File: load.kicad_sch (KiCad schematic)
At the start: 42 parts, among them IC3 TC4429CPA, IC4 TPS2121RUXR, J12 Conn_01x02_Socket, J13 Conn_01x02_Socket, J14 Conn_01x02_Socket, J16 Conn_01x02_Socket, J24 Conn_01x02_Socket, J3 Conn_01x02_Socket, J5 Conn_01x02_Socket, J9 Conn_01x03_Socket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

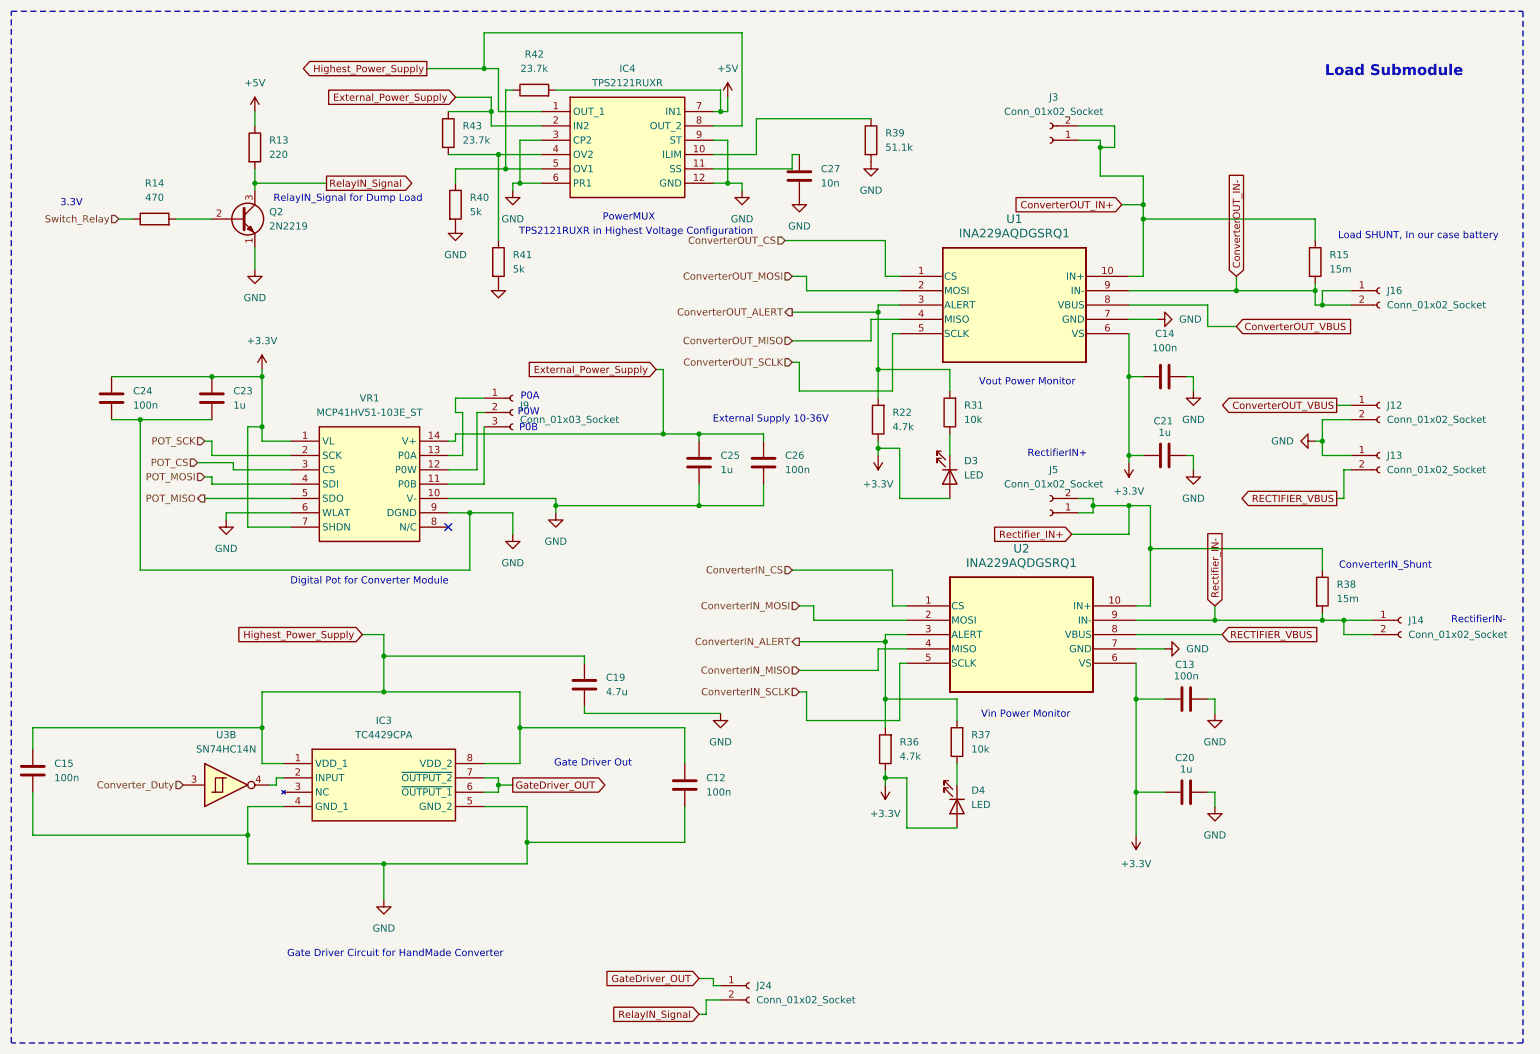
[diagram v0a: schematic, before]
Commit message: Added final changes to PCB: 1. Fixed OV2 ressitors on Power MUX, 2. Added input filtering on both INA229, 3. Changed the LDO layout based on manufacturer recomendations.
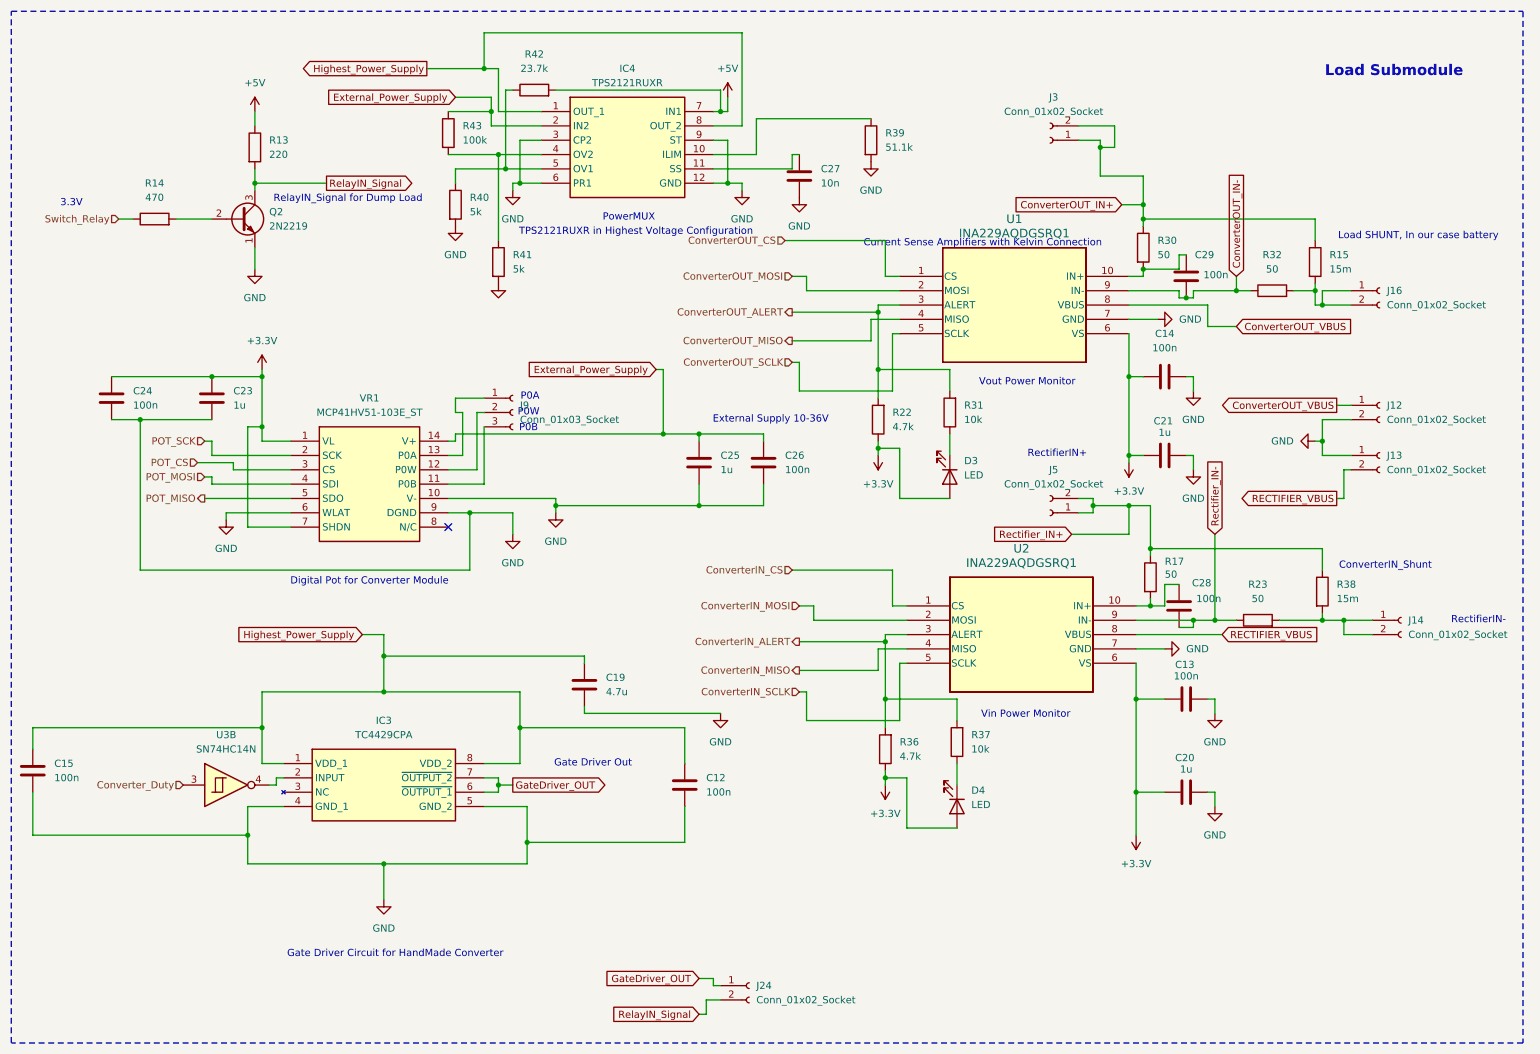
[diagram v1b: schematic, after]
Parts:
- added C28, C29: 100n, Capacitor_SMD:C_0402_1005Metric_Pad0.74x0.62mm_HandSolder, symbol Device:C
- added R17, R23, R30, R32: 50, Resistor_SMD:R_0402_1005Metric_Pad0.72x0.64mm_HandSolder, symbol Device:R
- R43: value 23.7k -> 100k
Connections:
- net ConverterOUT_IN+: now also R30.1; no longer U1.10 (IN+)
- net ConverterOUT_IN-: now also C29.2, R32.1; no longer J16.1 (Pin_1), J16.2 (Pin_2), R15.2
- net Rectifier_IN+: now also R17.1; no longer U2.10 (IN+)
- net Rectifier_IN-: now also C28.2, R23.1; no longer J14.1 (Pin_1), J14.2 (Pin_2), R38.2
- new net: C29.1, R30.2, U1.10 (IN+)
- new net: C28.1, R17.2, U2.10 (IN+)
- new net: J16.1 (Pin_1), J16.2 (Pin_2), R15.2, R32.2
- new net: J14.1 (Pin_1), J14.2 (Pin_2), R23.2, R38.2
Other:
- note added: "Current Sense Amplifiers with Kelvin Connection"

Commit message: Finished pcb for manufacturing, changed some footprints based on what the manufacturer had. Also I fixed the potentiometer footprint.
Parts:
- R39: value 51.1k -> 51k; footprint Resistor_SMD:R_1206_3216Metric_Pad1.30x1.75mm_HandSolder -> Resistor_SMD:R_0805_2012Metric_Pad1.20x1.40mm_HandSolder
- R40, R41: value 5k -> 4.7k
- R42: value 23.7k -> 24k; footprint Resistor_SMD:R_1206_3216Metric_Pad1.30x1.75mm_HandSolder -> Resistor_SMD:R_0805_2012Metric_Pad1.20x1.40mm_HandSolder
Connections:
- net ConverterOUT_IN-: now also J16.1 (Pin_1), J16.2 (Pin_2), R15.2, R32.2; no longer C29.2, R32.1, U1.9 (IN-)
- net Rectifier_IN-: now also J14.1 (Pin_1), J14.2 (Pin_2), R23.2, R38.2; no longer C28.2, R23.1, U2.9 (IN-)
- new net: C28.2, R23.1, U2.9 (IN-)
- new net: C29.2, R32.1, U1.9 (IN-)
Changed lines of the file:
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@@
 	)
 	(junction
-		(at 245.11 59.69)
+		(at 242.57 59.69)
 		(diameter 0)
 		(color 0 0 0 0)
 	)
 	(junction
-		(at 49.53 74.93)
+		(at 245.11 59.69)
 		(diameter 0)
 		(color 0 0 0 0)
 	)
 	(junction
-		(at 168.91 132.08)
+		(at 49.53 74.93)
 		(diameter 0)
 		(color 0 0 0 0)
 	)
 	(junction
-		(at 231.14 59.69)
+		(at 168.91 132.08)
 		(diameter 0)
 		(color 0 0 0 0)
@@
 	)
 	(junction
+		(at 241.3 118.11)
+		(diameter 0)
+		(color 0 0 0 0)
+	)
+	(junction
 		(at 246.38 86.36)
 		(diameter 0)
@@
 	)
 	(junction
-		(at 227.33 118.11)
-		(diameter 0)
-		(color 0 0 0 0)
-	)
-	(junction
 		(at 205.74 97.79)
 		(diameter 0)
@@
 	(wire
 		(pts
-			(xy 231.14 59.69) (xy 233.68 59.69)
+			(xy 223.52 59.69) (xy 233.68 59.69)
 		)
 		(stroke
@@
 	(wire
 		(pts
+			(xy 242.57 53.34) (xy 242.57 59.69)
+		)
+		(stroke
+			(width 0)
+			(type default)
+		)
+	)
+	(wire
+		(pts
 			(xy 138.43 182.88) (xy 138.43 181.61)
 		)
@@
 	(wire
 		(pts
-			(xy 223.52 59.69) (xy 231.14 59.69)
-		)
-		(stroke
-			(width 0)
-			(type default)
-		)
-	)
-	(wire
-		(pts
 			(xy 168.91 146.05) (xy 168.91 147.32)
 		)
@@
 	(wire
 		(pts
-			(xy 104.14 137.16) (xy 104.14 130.81)
+			(xy 241.3 118.11) (xy 246.38 118.11)
 		)
 		(stroke
@@
 	(wire
 		(pts
-			(xy 213.36 132.08) (xy 213.36 148.59)
+			(xy 104.14 137.16) (xy 104.14 130.81)
 		)
 		(stroke
@@
 	(wire
 		(pts
-			(xy 62.23 151.13) (xy 55.88 151.13)
+			(xy 213.36 132.08) (xy 213.36 148.59)
 		)
 		(stroke
@@
 	(wire
 		(pts
-			(xy 223.52 91.44) (xy 223.52 88.9)
+			(xy 62.23 151.13) (xy 55.88 151.13)
 		)
 		(stroke
@@
 	(wire
 		(pts
-			(xy 100.33 147.32) (xy 100.33 146.05)
+			(xy 223.52 91.44) (xy 223.52 88.9)
 		)
 		(stroke
@@
 	(wire
 		(pts
-			(xy 58.42 74.93) (xy 58.42 83.82)
+			(xy 100.33 147.32) (xy 100.33 146.05)
 		)
 		(stroke
@@
 	(wire
 		(pts
-			(xy 227.33 102.87) (xy 227.33 118.11)
+			(xy 58.42 74.93) (xy 58.42 83.82)
 		)
 		(stroke
@@
 	(wire
 		(pts
+			(xy 242.57 59.69) (xy 245.11 59.69)
+		)
+		(stroke
+			(width 0)
+			(type default)
+		)
+	)
+	(wire
+		(pts
 			(xy 133.35 143.51) (xy 133.35 137.16)
 		)
@@
 	(wire
 		(pts
+			(xy 241.3 113.03) (xy 241.3 118.11)
+		)
+		(stroke
+			(width 0)
+			(type default)
+		)
+	)
+	(wire
+		(pts
 			(xy 223.52 119.38) (xy 223.52 118.11)
 		)
@@
 	(wire
 		(pts
-			(xy 238.76 118.11) (xy 246.38 118.11)
+			(xy 238.76 118.11) (xy 241.3 118.11)
 		)
 		(stroke
@@
 	(wire
 		(pts
-			(xy 227.33 118.11) (xy 231.14 118.11)
+			(xy 223.52 118.11) (xy 231.14 118.11)
 		)
 		(stroke
@@
 	(wire
 		(pts
-			(xy 223.52 118.11) (xy 227.33 118.11)
-		)
-		(stroke
-			(width 0)
-			(type default)
-		)
-	)
-	(wire
-		(pts
 			(xy 147.32 86.36) (xy 147.32 85.09)
 		)
@@
 	(wire
 		(pts
-			(xy 241.3 59.69) (xy 245.11 59.69)
+			(xy 241.3 59.69) (xy 242.57 59.69)
 		)
 		(stroke
@@
 	(wire
 		(pts
-			(xy 231.14 57.15) (xy 231.14 59.69)
-		)
-		(stroke
-			(width 0)
-			(type default)
-		)
-	)
-	(wire
-		(pts
 			(xy 17.78 140.97) (xy 17.78 137.16)
 		)
@@
 		)
 	)
-	(global_label "ConverterOUT_IN-"
-		(shape input)
-		(at 231.14 57.15 90)
-		(fields_autoplaced yes)
-		(effects
-			(font
-				(size 1.27 1.27)
-			)
-			(justify left)
-		)
-		(property "Intersheetrefs" "${INTERSHEET_REFS}"
-			(at 231.14 37.05 90)
-			(effects
-				(font
-					(size 1.27 1.27)
-				)
-				(justify left)
-				(hide yes)
-			)
-		)
-	)
 	(global_label "Highest_Power_Supply"
 		(shape output)
@@
 	(global_label "Rectifier_IN-"
 		(shape input)
-		(at 227.33 102.87 90)
+		(at 241.3 113.03 90)
 		(fields_autoplaced yes)
 		(effects
@@
 		)
 		(property "Intersheetrefs" "${INTERSHEET_REFS}"
-			(at 227.33 87.4265 90)
+			(at 241.3 97.5865 90)
 			(effects
 				(font
@@
 		)
 	)
+	(global_label "ConverterOUT_IN-"
+		(shape input)
+		(at 242.57 53.34 90)
+		(fields_autoplaced yes)
+		(effects
+			(font
+				(size 1.27 1.27)
+			)
+			(justify left)
+		)
+		(property "Intersheetrefs" "${INTERSHEET_REFS}"
+			(at 242.57 33.24 90)
+			(effects
+				(font
+					(size 1.27 1.27)
+				)
+				(justify left)
+				(hide yes)
+			)
+		)
+	)
 	(global_label "ConverterOUT_VBUS"
 		(shape input)
@@
 			)
 		)
-		(property "Value" "5k"
+		(property "Value" "4.7k"
 			(at 95.25 45.7199 0)
 			(effects
@@
 			)
 		)
-		(property "Value" "5k"
+		(property "Value" "4.7k"
 			(at 102.87 55.8799 0)
 			(effects
@@
 			)
 		)
-		(property "Value" "51.1k"
+		(property "Value" "51k"
 			(at 168.91 34.2899 0)
 			(effects
@@
 			)
 		)
-		(property "Footprint" "Resistor_SMD:R_1206_3216Metric_Pad1.30x1.75mm_HandSolder"
+		(property "Footprint" "Resistor_SMD:R_0805_2012Metric_Pad1.20x1.40mm_HandSolder"
 			(at 164.592 33.02 90)
 			(effects
@@
 			)
 		)
-		(property "Value" "23.7k"
+		(property "Value" "24k"
 			(at 106.68 20.32 90)
 			(effects
@@
 			)
 		)
-		(property "Footprint" "Resistor_SMD:R_1206_3216Metric_Pad1.30x1.75mm_HandSolder"
+		(property "Footprint" "Resistor_SMD:R_0805_2012Metric_Pad1.20x1.40mm_HandSolder"
 			(at 106.68 25.908 90)
 			(effects

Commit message: Removed unnecessary hex inverter, fixed record button connection, change relay resistors to smd
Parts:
- added TP1, TP2: TestPoint, TestPoint:TestPoint_Pad_D1.0mm, symbol Connector:TestPoint
- R13, R14: footprint Resistor_THT:R_Axial_DIN0207_L6.3mm_D2.5mm_P7.62mm_Horizontal -> Resistor_SMD:R_0805_2012Metric_Pad1.20x1.40mm_HandSolder
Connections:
- net GND: now also TP2.1
- net Highest_Power_Supply: now also TP1.1
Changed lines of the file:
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@@
 	)
 	(junction
+		(at 97.79 17.78)
+		(diameter 0)
+		(color 0 0 0 0)
+	)
+	(junction
 		(at 212.09 74.93)
 		(diameter 0)
@@
 	)
 	(junction
+		(at 106.68 40.64)
+		(diameter 0)
+		(color 0 0 0 0)
+	)
+	(junction
 		(at 241.3 118.11)
 		(diameter 0)
@@
 	(wire
 		(pts
+			(xy 97.79 17.78) (xy 97.79 20.32)
+		)
+		(stroke
+			(width 0)
+			(type default)
+		)
+	)
+	(wire
+		(pts
 			(xy 223.52 59.69) (xy 233.68 59.69)
 		)
@@
 	(wire
 		(pts
+			(xy 153.67 77.47) (xy 170.18 77.47)
+		)
+		(stroke
+			(width 0)
+			(type default)
+		)
+	)
+	(wire
+		(pts
 			(xy 220.98 111.76) (xy 218.44 111.76)
 		)
@@
 	(wire
 		(pts
+			(xy 48.26 96.52) (xy 63.5 96.52)
+		)
+		(stroke
+			(width 0)
+			(type default)
+		)
+	)
+	(wire
+		(pts
 			(xy 207.01 39.37) (xy 214.63 39.37)
 		)
@@
 	(wire
 		(pts
+			(xy 46.99 90.17) (xy 53.34 90.17)
+		)
+		(stroke
+			(width 0)
+			(type default)
+		)
+	)
+	(wire
+		(pts
 			(xy 241.3 118.11) (xy 246.38 118.11)
 		)
@@
 	(wire
 		(pts
+			(xy 151.13 50.8) (xy 168.91 50.8)
+		)
+		(stroke
+			(width 0)
+			(type default)
+		)
+	)
+	(wire
+		(pts
 			(xy 213.36 132.08) (xy 213.36 148.59)
 		)
@@
 	(wire
 		(pts
-			(xy 104.14 40.64) (xy 107.95 40.64)
+			(xy 104.14 40.64) (xy 106.68 40.64)
 		)
 		(stroke
@@
 	(wire
 		(pts
+			(xy 106.68 41.91) (xy 106.68 40.64)
+		)
+		(stroke
+			(width 0)
+			(type default)
+		)
+	)
+	(wire
+		(pts
 			(xy 212.09 97.79) (xy 215.9 97.79)
 		)
@@
 	(wire
 		(pts
+			(xy 92.71 17.78) (xy 97.79 17.78)
+		)
+		(stroke
+			(width 0)
+			(type default)
+		)
+	)
+	(wire
+		(pts
 			(xy 156.21 118.11) (xy 156.21 115.57)
 		)
@@
 	(wire
 		(pts
-			(xy 97.79 13.97) (xy 97.79 20.32)
+			(xy 97.79 13.97) (xy 97.79 17.78)
 		)
 		(stroke
@@
 	(wire
 		(pts
-			(xy 246.38 105.41) (xy 246.38 109.22)
+			(xy 107.95 41.91) (xy 106.68 41.91)
 		)
 		(stroke
@@
 	(wire
 		(pts
-			(xy 213.36 148.59) (xy 213.36 156.21)
+			(xy 246.38 105.41) (xy 246.38 109.22)
 		)
 		(stroke
@@
 	(wire
 		(pts
-			(xy 156.21 115.57) (xy 153.67 115.57)
+			(xy 213.36 148.59) (xy 213.36 156.21)
 		)
 		(stroke
@@
 	(wire
 		(pts
-			(xy 214.63 39.37) (xy 214.63 44.45)
+			(xy 156.21 115.57) (xy 153.67 115.57)
 		)
 		(stroke
@@
 	(wire
 		(pts
-			(xy 48.26 96.52) (xy 63.5 96.52)
+			(xy 214.63 39.37) (xy 214.63 44.45)
 		)
 		(stroke
@@
 	(wire
 		(pts
-			(xy 153.67 77.47) (xy 170.18 77.47)
-		)
-		(stroke
-			(width 0)
-			(type default)
-		)
-	)
-	(wire
-		(pts
 			(xy 220.98 119.38) (xy 223.52 119.38)
 		)
@@
 	(wire
 		(pts
+			(xy 106.68 40.64) (xy 107.95 40.64)
+		)
+		(stroke
+			(width 0)
+			(type default)
+		)
+	)
+	(wire
+		(pts
 			(xy 214.63 57.15) (xy 212.09 57.15)
 		)
@@
 	(wire
 		(pts
-			(xy 151.13 50.8) (xy 168.91 50.8)
-		)
-		(stroke
-			(width 0)
-			(type default)
-		)
-	)
-	(wire
-		(pts
 			(xy 55.88 101.6) (xy 55.88 83.82)
 		)
@@
 	(wire
 		(pts
-			(xy 46.99 90.17) (xy 53.34 90.17)
-		)
-		(stroke
-			(width 0)
-			(type default)
-		)
-	)
-	(wire
-		(pts
 			(xy 250.19 118.11) (xy 255.27 118.11)
 		)
@@
 			)
 		)
-		(property "Footprint" "Resistor_THT:R_Axial_DIN0207_L6.3mm_D2.5mm_P7.62mm_Horizontal"
+		(property "Footprint" "Resistor_SMD:R_0805_2012Metric_Pad1.20x1.40mm_HandSolder"
 			(at 55.372 34.29 90)
 			(effects
@@
 	)
 	(symbol
+		(lib_id "Connector:TestPoint")
+		(at 92.71 17.78 90)
+		(unit 1)
+		(exclude_from_sim no)
+		(in_bom yes)
+		(on_board yes)
+		(dnp no)
+		(fields_autoplaced yes)
+		(property "Reference" "TP1"
+			(at 89.408 12.7 90)
+			(effects
+				(font
+					(size 1.27 1.27)
+				)
+			)
+		)
+		(property "Value" "TestPoint"
+			(at 89.408 15.24 90)
+			(effects
+				(font
+					(size 1.27 1.27)
+				)
+			)
+		)
+		(property "Footprint" "TestPoint:TestPoint_Pad_D1.0mm"
+			(at 92.71 12.7 0)
+			(effects
+				(font
+					(size 1.27 1.27)
+				)
+				(hide yes)
+			)
+		)
+		(property "Datasheet" "~"
+			(at 92.71 12.7 0)
+			(effects
+				(font
+					(size 1.27 1.27)
+				)
+				(hide yes)
+			)
+		)
+		(property "Description" "test point"
+			(at 92.71 17.78 0)
+			(effects
+				(font
+					(size 1.27 1.27)
+				)
+				(hide yes)
+			)
+		)
+		(pin "1"
+		)
+		(instances
+			(project ""
+				(path "/526b8b14-d04c-43b9-8d25-bcbd5ccf5c4d/67ed2c44-c453-42c8-aaa0-3d1863e73c07"
+					(reference "TP1")
+					(unit 1)
+				)
+			)
+		)
+	)
+	(symbol
 		(lib_id "power:+5V")
 		(at 57.15 27.94 0)
@@
 			)
 		)
-		(property "Footprint" "Resistor_THT:R_Axial_DIN0207_L6.3mm_D2.5mm_P7.62mm_Horizontal"
+		(property "Footprint" "Resistor_SMD:R_0805_2012Metric_Pad1.20x1.40mm_HandSolder"
 			(at 39.37 48.768 90)
 			(effects
@@
 					(unit 1)
 				)
+			)
+		)
+	)
+	(symbol
+		(lib_id "Connector:TestPoint")
+		(at 107.95 41.91 180)
+		(unit 1)
+		(exclude_from_sim no)
+		(in_bom yes)
+		(on_board yes)
+		(dnp no)
+		(fields_autoplaced yes)
+		(property "Reference" "TP2"
+			(at 110.49 43.9419 0)
+			(effects
+				(font
+					(size 1.27 1.27)
+				)
+				(justify right)
+			)
+		)
+		(property "Value" "TestPoint"
+			(at 110.49 46.4819 0)
+			(effects
+				(font
+					(size 1.27 1.27)
+				)
+				(justify right)
+			)
+		)
+		(property "Footprint" "TestPoint:TestPoint_Pad_D1.0mm"
+			(at 102.87 41.91 0)
+			(effects
+				(font
+					(size 1.27 1.27)
+				)
+				(hide yes)
+			)
+		)
+		(property "Datasheet" "~"
+			(at 102.87 41.91 0)
+			(effects
+				(font
+					(size 1.27 1.27)
+				)
+				(hide yes)
+			)
+		)
+		(property "Description" "test point"
+			(at 107.95 41.91 0)
+			(effects
+				(font
+					(size 1.27 1.27)
+				)
+				(hide yes)
+			)
+		)
+		(pin "1"
+		)
+		(instances
+			(project "Load-UI_MCU"
+				(path "/526b8b14-d04c-43b9-8d25-bcbd5ccf5c4d/67ed2c44-c453-42c8-aaa0-3d1863e73c07"
+					(reference "TP2")
+					(unit 1)
+				)

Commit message: schematic comments
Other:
- note added: "These INA229 design were based from TI and Adafruit EVM's"
- note added: "This gate driver has an inverted output, we could invert the PWM signal directly from the uC but I(Hiram) chose to use a spare inverter from the SN74HC14 instead"
- note added: "https://a.co/d/08Djs6OC"
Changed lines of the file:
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@@
+		)
+	)
+	(arc
+		(start 57.15 114.3)
+		(mid 57.9699 111.4023)
+		(end 60.96 111.76)
+		(stroke
+			(width 0)
+			(type default)
+		)
+		(fill
+			(type none)
+		)
+	)
+	(arc
+		(start 41.07 154.64)
+		(mid 41.8899 151.7423)
+		(end 44.88 152.1)
+		(stroke
+			(width 0)
+			(type default)
+		)
+		(fill
+			(type none)
 		)
 	)
@@
 		)
 	)
+	(text "These INA229 design were based from TI and Adafruit EVM's"
+		(exclude_from_sim no)
+		(at 176.276 158.242 0)
+		(effects
+			(font
+				(size 1.27 1.27)
+			)
+		)
+	)
 	(text "PowerMUX"
 		(exclude_from_sim no)
@@
 		)
 	)
+	(text "This gate driver has an inverted output,\nwe could invert the PWM signal directly from the uC but I(Hiram)\nchose to use a spare inverter from the SN74HC14 instead"
+		(exclude_from_sim no)
+		(at 14.986 160.274 0)
+		(effects
+			(font
+				(size 1.27 1.27)
+			)
+			(justify left)
+		)
+	)
 	(text "ConverterIN_Shunt"
 		(exclude_from_sim no)
@@
 		(exclude_from_sim no)
 		(at 82.042 177.292 0)
+		(effects
+			(font
+				(size 1.27 1.27)
+			)
+		)
+	)
+	(text "https://a.co/d/08Djs6OC"
+		(exclude_from_sim no)
+		(at 68.072 115.824 0)
 		(effects
 			(font
@@
 		)
 	)
+	(polyline
+		(pts
+			(xy 59.69 111.76) (xy 60.96 111.76)
+		)
+		(stroke
+			(width 0)
+			(type default)
+		)
+	)
 	(wire
 		(pts
@@
 		)
 	)
+	(polyline
+		(pts
+			(xy 60.96 110.49) (xy 60.96 111.76)
+		)
+		(stroke
+			(width 0)
+			(type default)
+		)
+	)
 	(wire
 		(pts
@@
 		)
 	)
+	(polyline
+		(pts
+			(xy 43.61 152.1) (xy 44.88 152.1)
+		)
+		(stroke
+			(width 0)
+			(type default)
+		)
+	)
 	(wire
 		(pts
@@
 		)
 		(stroke
+			(width 0)
+			(type default)
+		)
+	)
+	(polyline
+		(pts
+			(xy 44.88 150.83) (xy 44.88 152.1)
+		)
+		(stroke
